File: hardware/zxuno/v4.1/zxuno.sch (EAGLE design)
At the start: 103 parts, among them T1 BC846, U1 6SLX9TQG144, U2 FLASH-SPI-25XXSMD1, U4 AD724, U5 50MHz, U6 3.3V, U7 1.2V, Y1 3.58M, Y2 4.43M

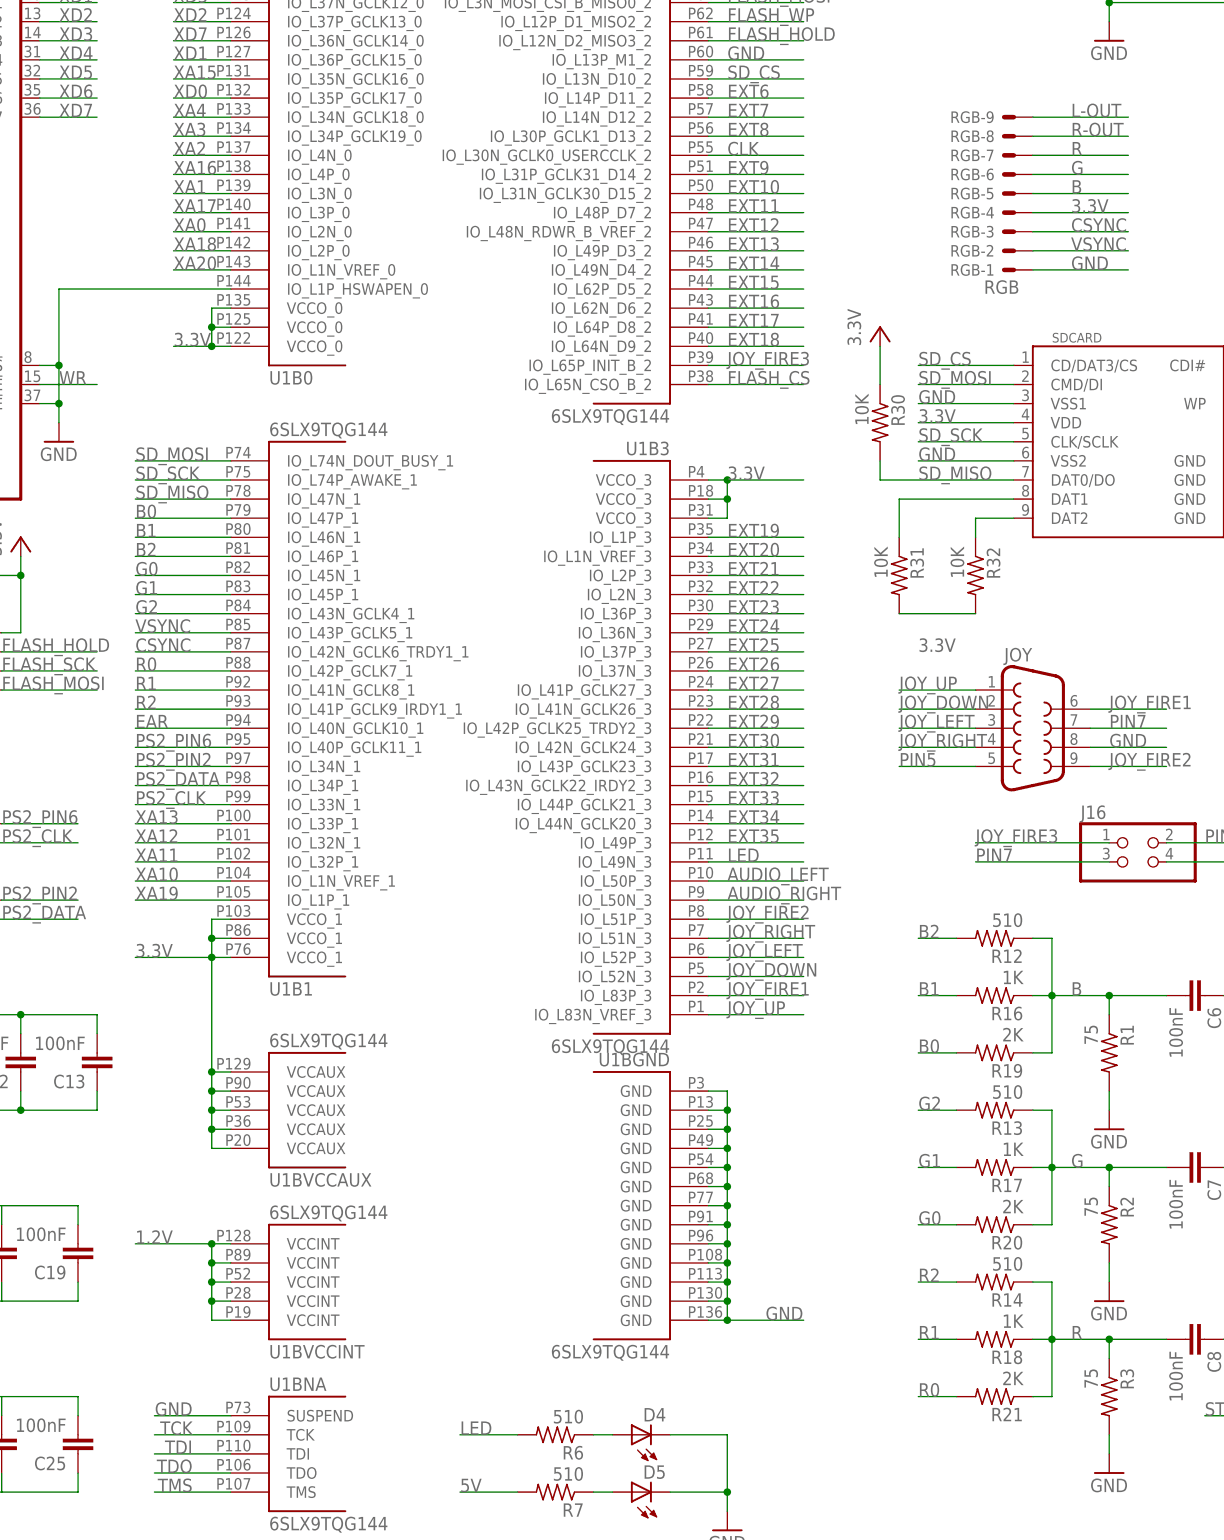
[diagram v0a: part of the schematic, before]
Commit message: 4- Las señales "R in" y "B in" del AD724 están intercambiadas y el color por video compuesto sale mal (por RGB sale bien). Corregir
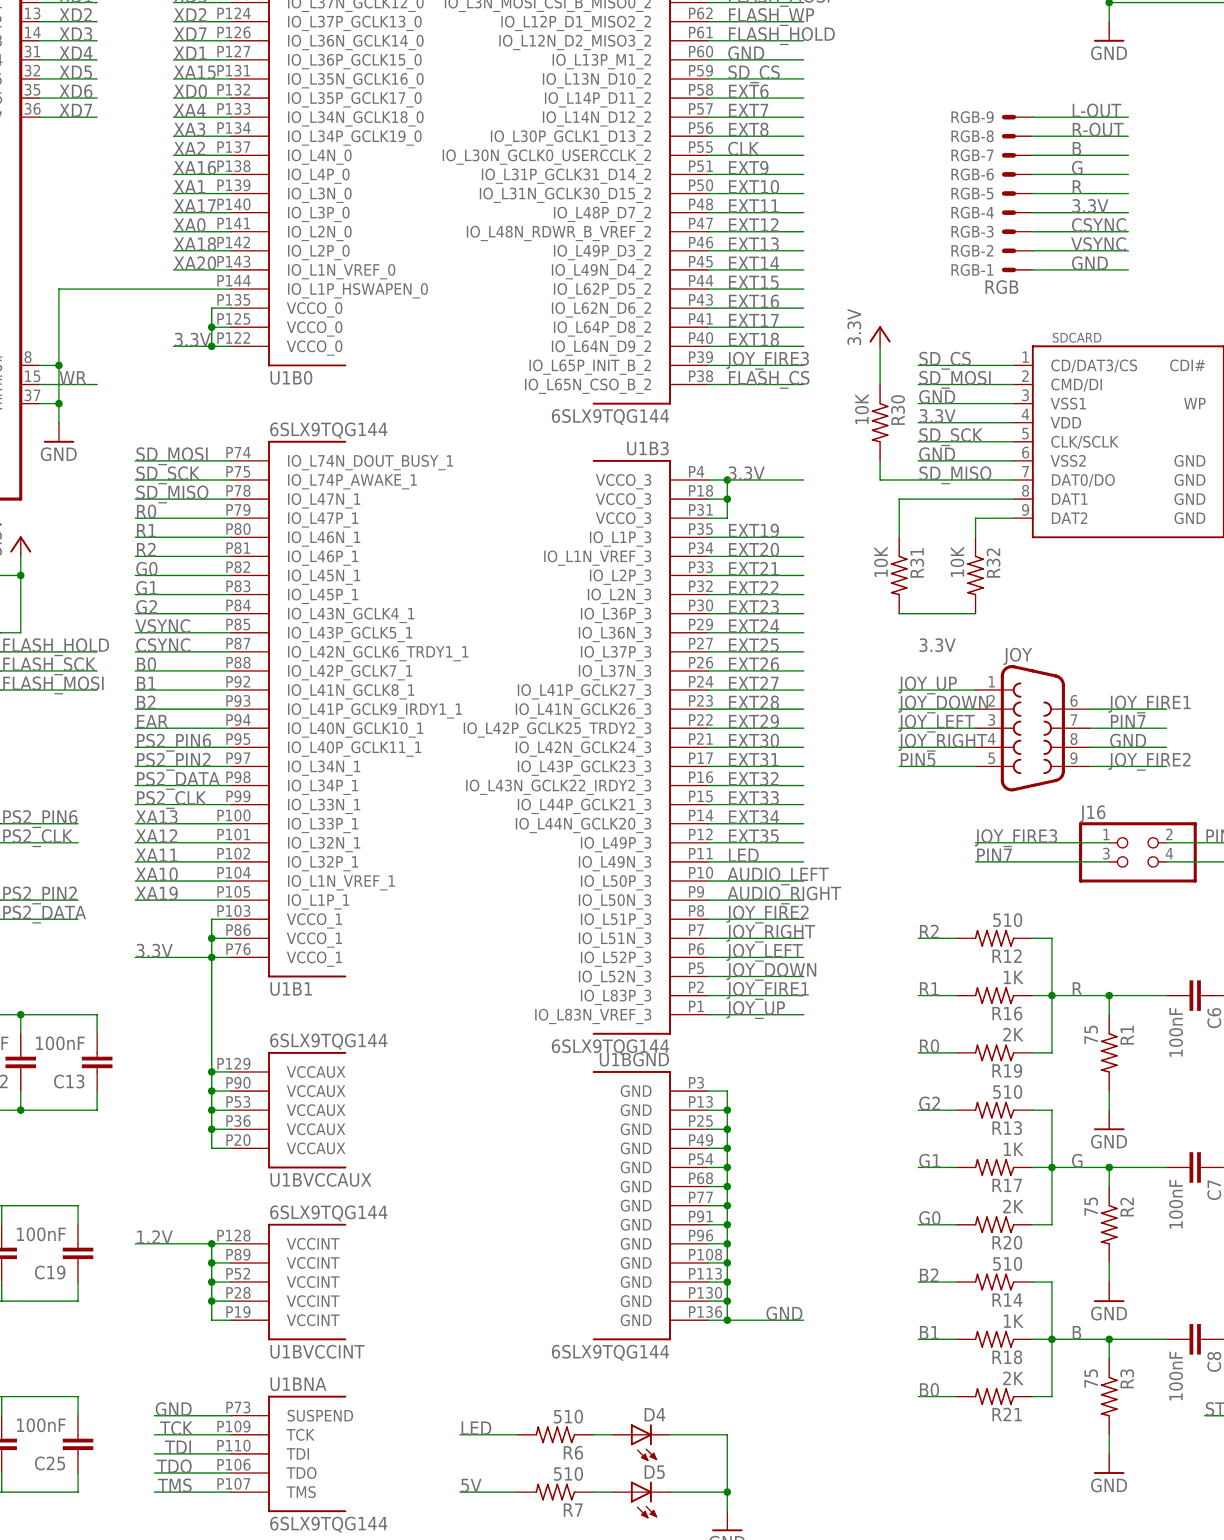
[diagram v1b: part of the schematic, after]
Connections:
- net B: now also C8.2, R14.1, R18.1, R21.1, R3.1, RGB-7.S; no longer C6.2, R1.1, R12.1, R16.1, R19.1, RGB-5.S
- net B0: now also R21.2, U1B1.IO_L42P_GCLK7_1; no longer R19.2, U1B1.IO_L47P_1
- net B1: now also R18.2, U1B1.IO_L41N_GCLK8_1; no longer R16.2, U1B1.IO_L46N_1
- net B2: now also R14.2, U1B1.IO_L41P_GCLK9_IRDY1_1; no longer R12.2, U1B1.IO_L46P_1
- net R: now also C6.2, R1.1, R12.1, R16.1, R19.1, RGB-5.S; no longer C8.2, R14.1, R18.1, R21.1, R3.1, RGB-7.S
- net R0: now also R19.2, U1B1.IO_L47P_1; no longer R21.2, U1B1.IO_L42P_GCLK7_1
- net R1: now also R16.2, U1B1.IO_L46N_1; no longer R18.2, U1B1.IO_L41N_GCLK8_1
- net R2: now also R12.2, U1B1.IO_L46P_1; no longer R14.2, U1B1.IO_L41P_GCLK9_IRDY1_1
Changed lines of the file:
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@@
 </segment>
 </net>
-<net name="B0" class="0">
+<net name="R0" class="0">
 <segment>
 <wire x1="35.56" y1="-7.62" x2="22.86" y2="-7.62" width="0.1524" layer="91"/>
@@
 </segment>
 </net>
-<net name="B1" class="0">
+<net name="R1" class="0">
 <segment>
 <wire x1="35.56" y1="-10.16" x2="22.86" y2="-10.16" width="0.1524" layer="91"/>
@@
 </segment>
 </net>
-<net name="B2" class="0">
+<net name="R2" class="0">
 <segment>
 <wire x1="35.56" y1="-12.7" x2="22.86" y2="-12.7" width="0.1524" layer="91"/>
@@
 </segment>
 </net>
-<net name="R0" class="0">
+<net name="B0" class="0">
 <segment>
 <wire x1="35.56" y1="-27.94" x2="22.86" y2="-27.94" width="0.1524" layer="91"/>
@@
 </segment>
 </net>
-<net name="R1" class="0">
+<net name="B1" class="0">
 <segment>
 <wire x1="35.56" y1="-30.48" x2="22.86" y2="-30.48" width="0.1524" layer="91"/>
@@
 </segment>
 </net>
-<net name="R2" class="0">
+<net name="B2" class="0">
 <segment>
 <wire x1="35.56" y1="-33.02" x2="22.86" y2="-33.02" width="0.1524" layer="91"/>
@@
 </segment>
 </net>
-<net name="B" class="0">
+<net name="R" class="0">
 <segment>
 <wire x1="154.94" y1="35.56" x2="142.24" y2="35.56" width="0.1524" layer="91"/>
@@
 </segment>
 </net>
-<net name="R" class="0">
+<net name="B" class="0">
 <segment>
 <pinref part="R14" gate="G$1" pin="1"/>

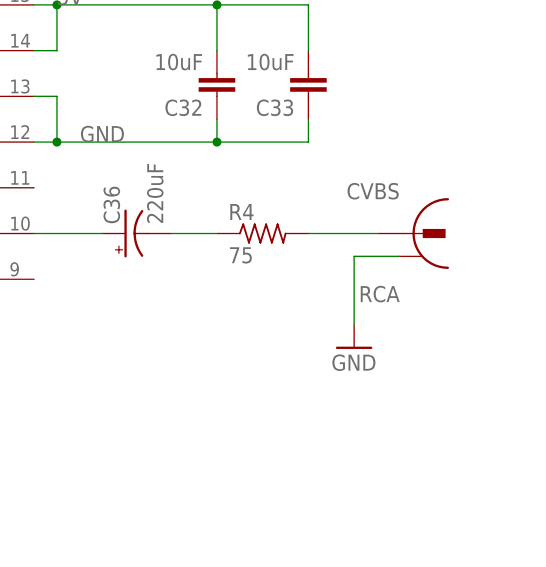
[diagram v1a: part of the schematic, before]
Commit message: 6- RCA video compuesto: El agujero de la pata trasera es del mismo tamaño que la pata. No entra y hay que limar 0.5mm para que entre
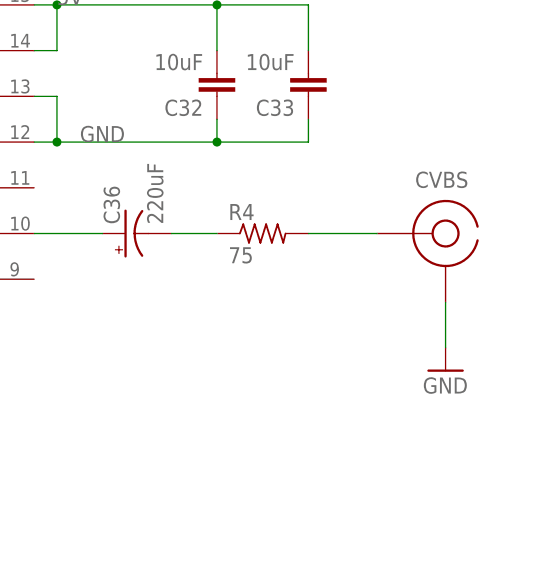
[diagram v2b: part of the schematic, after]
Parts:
- CVBS: device ZX_UNO_0_15:RCA_JACK_RCJ-04X_-_DUPLICATE_1 -> uzebox:RCA
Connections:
- net GND: now also CVBS.GND; no longer CVBS.2
- net N$28: now also CVBS.SIG; no longer CVBS.1
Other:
- moved on the sheet: CVBS
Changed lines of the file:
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@@
 <part name="PWCON" library="pinhead" deviceset="PINHD-1X2" device=""/>
 <part name="PS/2" library="ZX_UNO_0_14" deviceset="DINC_MIN_TM_6_1" device="" value="PS/2 Keyb"/>
-<part name="CVBS" library="ZX_UNO_0_15" deviceset="RCA_JACK_RCJ-04X_-_DUPLICATE_1" device="" value="RCA"/>
 <part name="U5" library="ZX_UNO_0_15" deviceset="SM_OSC_1" device="" value="50MHz"/>
 <part name="D1" library="adafruit" deviceset="DIODE" device="SOD-323F"/>
@@
 <part name="R32" library="rcl" deviceset="R-US_" device="M0805" value="10K"/>
 <part name="J16" library="pinhead" deviceset="PINHD-2X2" device=""/>
+<part name="CVBS" library="uzebox" deviceset="RCA" device=""/>
 </parts>
 <sheets>
@@
 <instance part="GND12" gate="1" x="177.8" y="-96.52"/>
 <instance part="C36" gate="G$1" x="241.3" y="-104.14" rot="R90"/>
-<instance part="GND13" gate="1" x="266.7" y="-116.84"/>
+<instance part="GND13" gate="1" x="276.86" y="-119.38"/>
 <instance part="R6" gate="G$1" x="78.74" y="-129.54" rot="R180"/>
 <instance part="R7" gate="G$1" x="78.74" y="-137.16" rot="R180"/>
@@
 <instance part="PWCON" gate="G$1" x="205.74" y="7.62" rot="R180"/>
 <instance part="PS/2" gate="G$1" x="-25.4" y="-55.88"/>
-<instance part="CVBS" gate="G$1" x="274.32" y="-104.14" rot="MR0"/>
 <instance part="U5" gate="G$1" x="0" y="81.28"/>
 <instance part="D1" gate="G$1" x="193.04" y="71.12" rot="R90"/>
@@
 <instance part="R32" gate="G$1" x="134.62" y="-15.24" rot="R270"/>
 <instance part="J16" gate="A" x="157.48" y="-53.34"/>
+<instance part="CVBS" gate="G$1" x="276.86" y="-104.14" rot="MR0"/>
 </instances>
 <busses>
@@
 <segment>
 <pinref part="GND13" gate="1" pin="GND"/>
-<wire x1="266.7" y1="-114.3" x2="266.7" y2="-106.68" width="0.1524" layer="91"/>
-<wire x1="266.7" y1="-106.68" x2="271.78" y2="-106.68" width="0.1524" layer="91"/>
-<pinref part="CVBS" gate="G$1" pin="2"/>
+<wire x1="276.86" y1="-116.84" x2="276.86" y2="-111.76" width="0.1524" layer="91"/>
+<pinref part="CVBS" gate="G$1" pin="GND"/>
 </segment>
 <segment>
@@
 <pinref part="R4" gate="G$1" pin="2"/>
 <wire x1="269.24" y1="-104.14" x2="261.62" y2="-104.14" width="0.1524" layer="91"/>
-<pinref part="CVBS" gate="G$1" pin="1"/>
-</segment>
-</net>
+<pinref part="CVBS" gate="G$1" pin="SIG"/>
+</segment>
+</net>

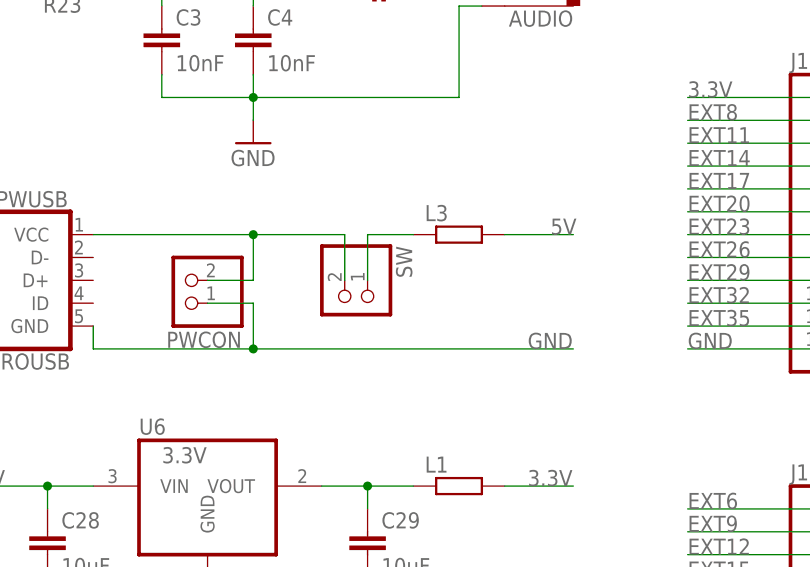
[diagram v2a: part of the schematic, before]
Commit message: v4.1 algunos aljustes en serigrafías
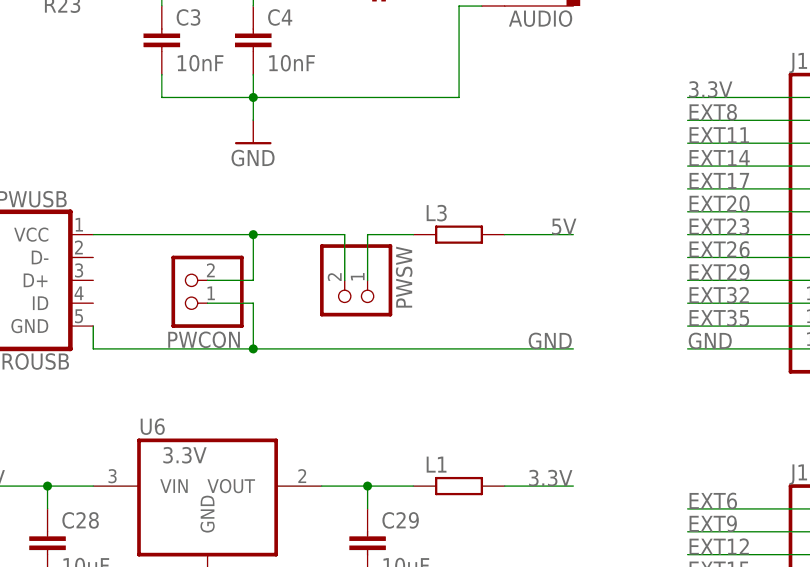
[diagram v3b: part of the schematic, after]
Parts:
- renumbered SW to PWSW
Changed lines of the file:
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@@
 <classes>
 <class number="0" name="default" width="0" drill="0">
+<clearance class="0" value="0.205"/>
 </class>
 </classes>
@@
 <part name="JTAG" library="con-molex" deviceset="53?-06" device="047" value="JTAG"/>
 <part name="RST" library="pinhead" deviceset="PINHD-1X2" device=""/>
-<part name="SW" library="pinhead" deviceset="PINHD-1X2" device=""/>
+<part name="PWSW" library="pinhead" deviceset="PINHD-1X2" device=""/>
 <part name="PWCON" library="pinhead" deviceset="PINHD-1X2" device=""/>
 <part name="PS/2" library="ZX_UNO_0_14" deviceset="DINC_MIN_TM_6_1" device="" value="PS/2 Keyb"/>
@@
 <instance part="JTAG" gate="-6" x="274.32" y="83.82"/>
 <instance part="RST" gate="G$1" x="119.38" y="68.58" rot="R270"/>
-<instance part="SW" gate="G$1" x="223.52" y="5.08" rot="R270"/>
+<instance part="PWSW" gate="G$1" x="223.52" y="5.08" rot="R270"/>
 <instance part="PWCON" gate="G$1" x="205.74" y="7.62" rot="R180"/>
 <instance part="PS/2" gate="G$1" x="-25.4" y="-55.88"/>
@@
 <pinref part="PWCON" gate="G$1" pin="2"/>
 <wire x1="208.28" y1="7.62" x2="213.36" y2="7.62" width="0.1524" layer="91"/>
-<pinref part="SW" gate="G$1" pin="2"/>
+<pinref part="PWSW" gate="G$1" pin="2"/>
 <wire x1="223.52" y1="7.62" x2="223.52" y2="12.7" width="0.1524" layer="91"/>
 <pinref part="PWUSB" gate="G$1" pin="VCC"/>
@@
 <pinref part="L3" gate="G$1" pin="1"/>
 <wire x1="231.14" y1="12.7" x2="226.06" y2="12.7" width="0.1524" layer="91"/>
-<pinref part="SW" gate="G$1" pin="1"/>
+<pinref part="PWSW" gate="G$1" pin="1"/>
 <wire x1="226.06" y1="7.62" x2="226.06" y2="12.7" width="0.1524" layer="91"/>
 </segment>
